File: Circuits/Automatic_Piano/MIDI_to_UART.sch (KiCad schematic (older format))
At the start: 6 parts

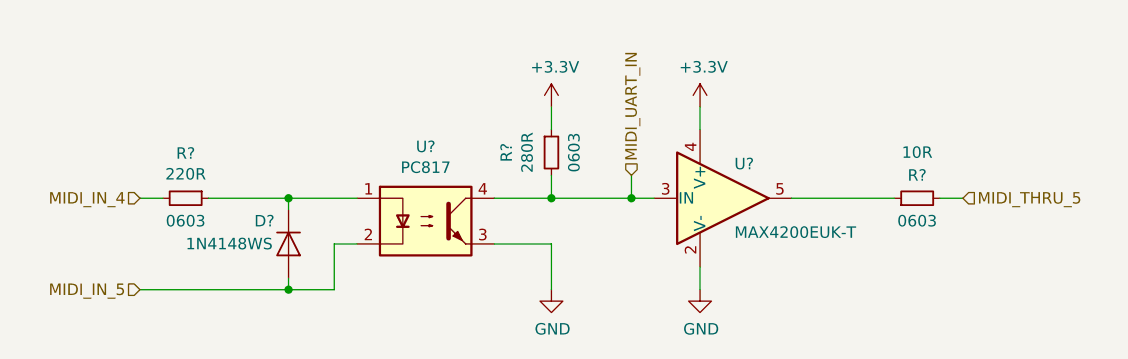
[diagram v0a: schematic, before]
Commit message: Main Piano MIDI receiver completed. Might want indicator LEDS and more peripherals.
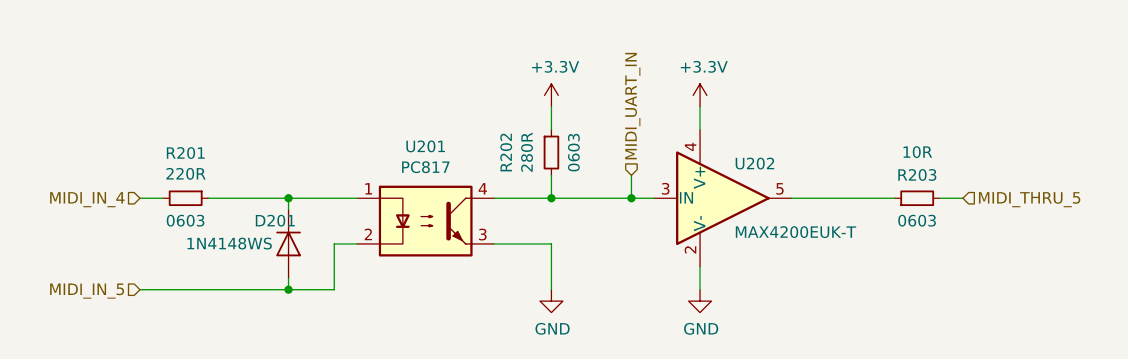
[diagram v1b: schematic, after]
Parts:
- gave numbers to parts that had none: 6
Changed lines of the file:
@@
 	3300 3200 3400 3200
 $Comp
-L Isolator:PC817 U?
+L Isolator:PC817 U201
 U 1 1 5E1ACB9A
 P 3700 3100
-F 0 "U?" H 3700 3425 50  0000 C CNN
+F 0 "U201" H 3700 3425 50  0000 C CNN
 F 1 "PC817" H 3700 3334 50  0000 C CNN
 F 2 "Package_DIP:DIP-4_W7.62mm" H 3500 2900 50  0001 L CIN
@@
 $EndComp
 $Comp
-L Device:R_Small R?
+L Device:R_Small R201
 U 1 1 5E1A338A
 P 2650 3000
-F 0 "R?" V 2454 3000 50  0000 C CNN
+F 0 "R201" V 2454 3000 50  0000 C CNN
 F 1 "220R" V 2545 3000 50  0000 C CNN
 F 2 "Resistor_SMD:R_0603_1608Metric" H 2650 3000 50  0001 C CNN
@@
 $EndComp
 $Comp
-L Device:D D?
+L Device:D D201
 U 1 1 5E1A5115
 P 3100 3200
-F 0 "D?" V 3000 3050 50  0000 L CNN
+F 0 "D201" V 3000 3050 50  0000 L CNN
 F 1 "1N4148WS" V 3100 2750 50  0000 L CNN
 F 2 "" H 3100 3200 50  0001 C CNN
@@
 	3100 3000 3400 3000
 $Comp
-L Device:R_Small R?
+L Device:R_Small R202
 U 1 1 5E1B355A
 P 4250 2800
-F 0 "R?" V 4054 2800 50  0000 C CNN
+F 0 "R202" V 4054 2800 50  0000 C CNN
 F 1 "280R" V 4145 2800 50  0000 C CNN
 F 2 "Resistor_SMD:R_0603_1608Metric" H 4250 2800 50  0001 C CNN
@@
 	4600 3000 4600 2900
 $Comp
-L Amplifier_Buffer:MAX4200EUK-T U?
+L Amplifier_Buffer:MAX4200EUK-T U202
 U 1 1 5E1B7735
 P 5000 3000
-F 0 "U?" H 5050 3150 50  0000 L CNN
+F 0 "U202" H 5050 3150 50  0000 L CNN
 F 1 "MAX4200EUK-T" H 5050 2850 50  0000 L CNN
 F 2 "Package_TO_SOT_SMD:SOT-23-5" H 5650 2700 50  0001 C CNN
@@
 	4600 3000 4700 3000
 $Comp
-L power:GND #PWR?
+L power:GND #PWR0204
 U 1 1 5E1BC356
 P 4900 3400
-F 0 "#PWR?" H 4900 3150 50  0001 C CNN
+F 0 "#PWR0204" H 4900 3150 50  0001 C CNN
 F 1 "GND" H 4905 3227 50  0000 C CNN
 F 2 "" H 4900 3400 50  0001 C CNN
@@
 	4900 2600 4900 2700
 $Comp
-L Device:R_Small R?
+L Device:R_Small R203
 U 1 1 5E1E1394
 P 5850 3000
-F 0 "R?" V 5950 3000 50  0000 C CNN
+F 0 "R203" V 5950 3000 50  0000 C CNN
 F 1 "10R" V 6050 3000 50  0000 C CNN
 F 2 "Resistor_SMD:R_0603_1608Metric" H 5850 3000 50  0001 C CNN
@@
 	5950 3000 6050 3000
 $Comp
-L power:+3.3V #PWR?
+L power:+3.3V #PWR0201
 U 1 1 5E1FE6BB
 P 4250 2600
-F 0 "#PWR?" H 4250 2450 50  0001 C CNN
+F 0 "#PWR0201" H 4250 2450 50  0001 C CNN
 F 1 "+3.3V" H 4265 2773 50  0000 C CNN
 F 2 "" H 4250 2600 50  0001 C CNN
@@
 $EndComp
 $Comp
-L power:+3.3V #PWR?
+L power:+3.3V #PWR0203
 U 1 1 5E1FFC39
 P 4900 2600
-F 0 "#PWR?" H 4900 2450 50  0001 C CNN
+F 0 "#PWR0203" H 4900 2450 50  0001 C CNN
 F 1 "+3.3V" H 4915 2773 50  0000 C CNN
 F 2 "" H 4900 2600 50  0001 C CNN
@@
 $EndComp
 $Comp
-L power:GND #PWR?
+L power:GND #PWR0202
 U 1 1 5E1B988A
 P 4250 3400
-F 0 "#PWR?" H 4250 3150 50  0001 C CNN
+F 0 "#PWR0202" H 4250 3150 50  0001 C CNN
 F 1 "GND" H 4255 3227 50  0000 C CNN
 F 2 "" H 4250 3400 50  0001 C CNN
